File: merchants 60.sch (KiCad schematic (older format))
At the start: 182 parts, among them SW1 SW_PUSH, U1 ATmega32U4-AU, Y1 16MHz

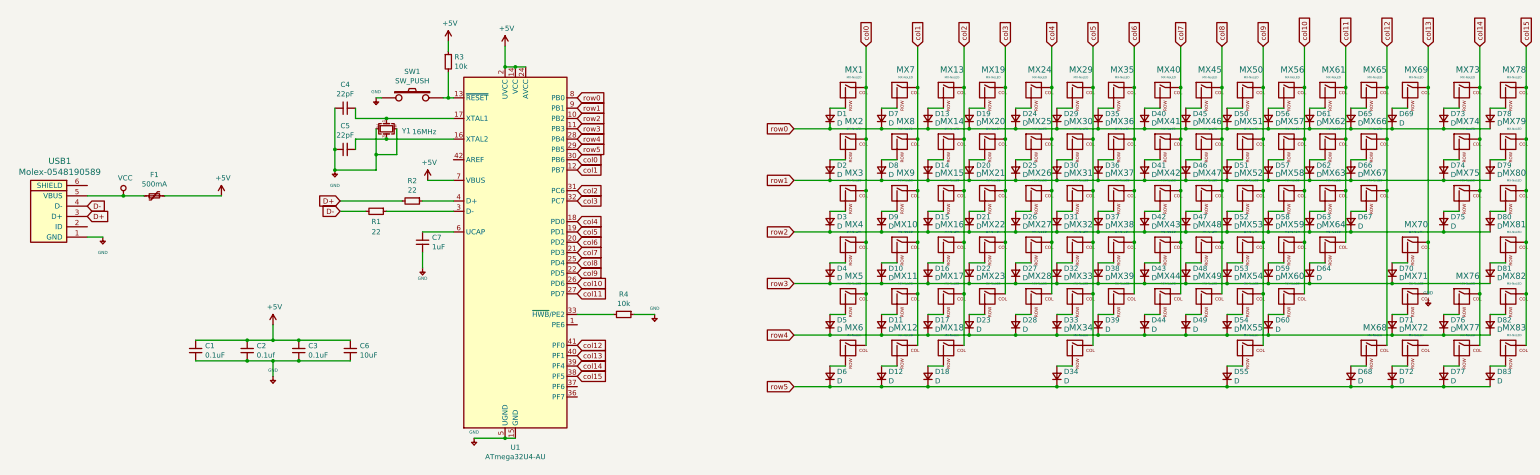
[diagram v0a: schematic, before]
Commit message: Finalising PCB and Generating Gerbers
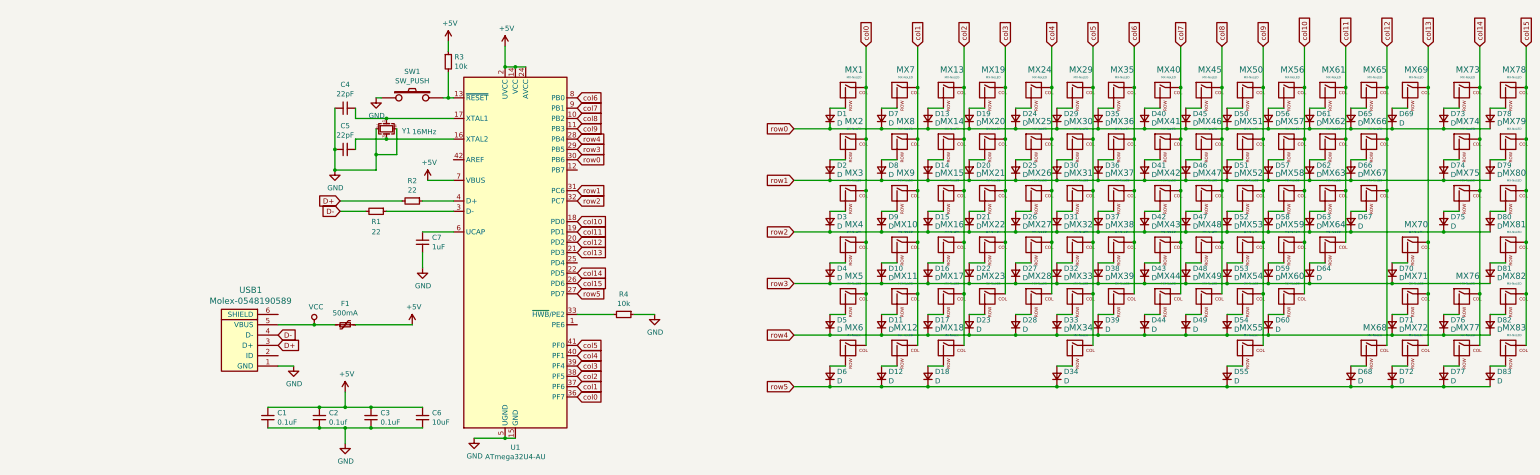
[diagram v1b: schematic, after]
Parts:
- D1, D10, D11, D12, D13, D14, D15, D16, D17, D18, D19, D2, D20, D21, D22, D23, D24, D25, D26, D27, D28, D29, D3, D30, D31, D32, D33, D34, D35, D36, D37, D38, D39, D4, D40, D41, D42, D43, D44, D45, D46, D47, D48, D49, D5, D50, D51, D52, D53, D54, D55, D56, D57, D58, D59, D6, D60, D61, D62, D63, D64, D65, D66, D67, D68, D69, D7, D70, D71, D72, D73, D74, D75, D76, D77, D78, D79, D8, D80, D81, D82, D83, D9: footprint Diode_SMD:D_SOD-123 -> keyboard_parts:D_SOD123_axial
- MX1, MX10, MX11, MX13, MX14, MX15, MX16, MX17, MX19, MX2, MX20, MX22, MX23, MX24, MX25, MX26, MX28, MX29, MX30, MX31, MX32, MX33, MX35, MX36, MX37, MX38, MX39, MX40, MX41, MX42, MX43, MX44, MX45, MX46, MX47, MX48, MX49, MX50, MX51, MX52, MX53, MX54, MX56, MX57, MX58, MX59, MX60, MX61, MX62, MX63, MX64, MX65, MX66, MX67, MX69, MX7, MX72, MX73, MX76, MX77, MX78, MX79, MX8, MX80, MX81, MX82, MX83, MX9: footprint (none) -> MX_Alps_Hybrid:MX-1U-NoLED
- MX12, MX18: footprint (none) -> MX_Alps_Hybrid:MX-1.25U-NoLED
- MX21, MX27: footprint MX_Alps_Hybrid:MX-1.25U -> MX_Alps_Hybrid:MX-1U-NoLED
- MX3, MX55, MX68, MX75: footprint MX_Alps_Hybrid:MX-1.5U -> MX_Alps_Hybrid:MX-1.5U-NoLED
- MX34: footprint MX_Alps_Hybrid:MX-6.25U -> MX_Alps_Hybrid:MX-6.25U-NoLED
- MX4, MX71: footprint MX_Alps_Hybrid:MX-1.75U -> MX_Alps_Hybrid:MX-1.75U-NoLED
- MX5: footprint MX_Alps_Hybrid:MX-2.5U -> MX_Alps_Hybrid:MX-2.25U-NoLED
- MX6: footprint MX_Alps_Hybrid:MX-1.25U -> MX_Alps_Hybrid:MX-1.25U-NoLED
- MX70: footprint MX_Alps_Hybrid:MX-2.25U -> MX_Alps_Hybrid:MX-2.25U-NoLED
- MX74: footprint MX_Alps_Hybrid:MX-2U -> MX_Alps_Hybrid:MX-2U-NoLED
- USB1: footprint random-keyboard-parts:Molex-0548190589 -> keyboard_parts:USB_miniB
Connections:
- net +5V: no longer C1.2, C2.2, C3.1, C4.2, C5.1, C6.2, C7.2, R4.1, SW1.1, U1.15 (GND), U1.23 (GND), U1.35 (GND), U1.43 (GND), U1.5 (UGND), USB1.1 (GND), Y1.2, Y1.4
- net col0: now also U1.36 (PF7); no longer U1.30 (PB6)
- net col1: now also U1.37 (PF6); no longer U1.12 (PB7)
- net col10: now also U1.18 (PD0); no longer U1.26 (PD6)
- net col11: now also U1.19 (PD1); no longer U1.27 (PD7)
- net col12: now also U1.20 (PD2); no longer U1.41 (PF0)
- net col13: now also MX72.1 (COL), U1.21 (PD3); no longer U1.40 (PF1)
- net col14: now also U1.22 (PD5); no longer U1.39 (PF4)
- net col15: now also U1.26 (PD6); no longer U1.38 (PF5)
- net col2: now also U1.38 (PF5); no longer U1.31 (PC6)
- net col3: now also U1.39 (PF4); no longer U1.32 (PC7)
- net col4: now also U1.40 (PF1); no longer U1.18 (PD0)
- net col5: now also U1.41 (PF0); no longer U1.19 (PD1)
- net col6: now also U1.8 (PB0); no longer U1.20 (PD2)
- net col7: now also U1.9 (PB1); no longer U1.21 (PD3)
- net col8: now also U1.10 (PB2); no longer U1.25 (PD4)
- net col9: now also U1.11 (PB3); no longer U1.22 (PD5)
- net row0: now also U1.30 (PB6); no longer U1.8 (PB0)
- net row1: now also U1.31 (PC6); no longer U1.9 (PB1)
- net row2: now also U1.32 (PC7); no longer U1.10 (PB2)
- net row3: now also U1.29 (PB5); no longer U1.11 (PB3)
- net row5: now also U1.27 (PD7); no longer U1.29 (PB5)
- new net GND: C1.2, C2.2, C3.1, C4.2, C5.1, C6.2, C7.2, R4.1, SW1.1, U1.15 (GND), U1.23 (GND), U1.35 (GND), U1.43 (GND), U1.5 (UGND), USB1.1 (GND), Y1.2, Y1.4
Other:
- moved on the sheet: C1, C2, C3, C6, F1, USB1

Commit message: Minor Changes
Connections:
- net row3: now also U1.27 (PD7); no longer U1.29 (PB5)
- net row5: now also U1.29 (PB5); no longer U1.27 (PD7)
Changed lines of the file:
@@
 row2
 Text GLabel 7550 2600 2    50   Input ~ 0
-row3
-Text GLabel 7550 2500 2    50   Input ~ 0
-row4
-Text GLabel 7550 4000 2    50   Input ~ 0
 row5
 Connection ~ 6850 5400
@@
 Text GLabel 7550 3900 2    50   Input ~ 0
 col15
-Text GLabel 7550 4500 2    50   Input ~ 0
-col5
 Text GLabel 7550 4600 2    50   Input ~ 0
 col4
@@
 Text GLabel 7550 4900 2    50   Input ~ 0
 col1
+Text GLabel 7550 4000 2    50   Input ~ 0
+row3
+Text GLabel 7550 2500 2    50   Input ~ 0
+row4
+Text GLabel 7550 4500 2    50   Input ~ 0
+col5
 $EndSCHEMATC

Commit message: Minor Changes
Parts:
- SW1: symbol keyboard_parts:SW_PUSH -> merchants-60-rescue:SW_PUSH-keyboard_parts
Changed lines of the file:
@@
 	5600 2650 5600 2400
 $Comp
-L keyboard_parts:SW_PUSH SW1
+L merchants-60-rescue:SW_PUSH-keyboard_parts SW1
 U 1 1 5F720C2E
 P 5950 2100

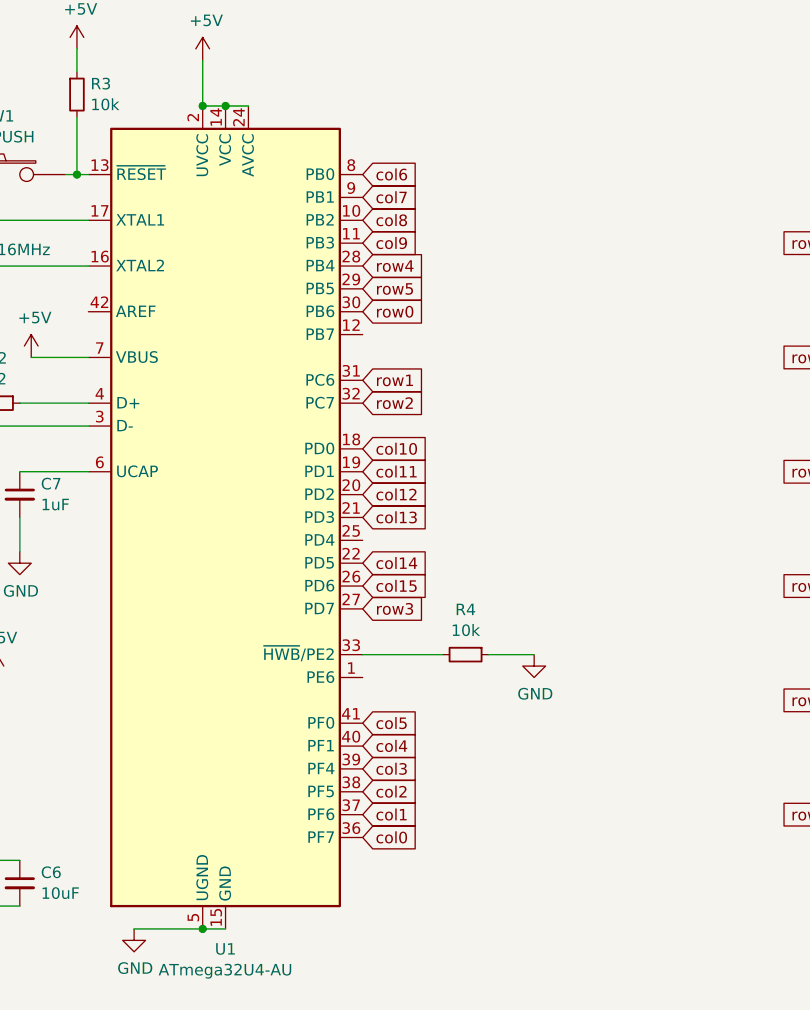
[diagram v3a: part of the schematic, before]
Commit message: Rerouting traces
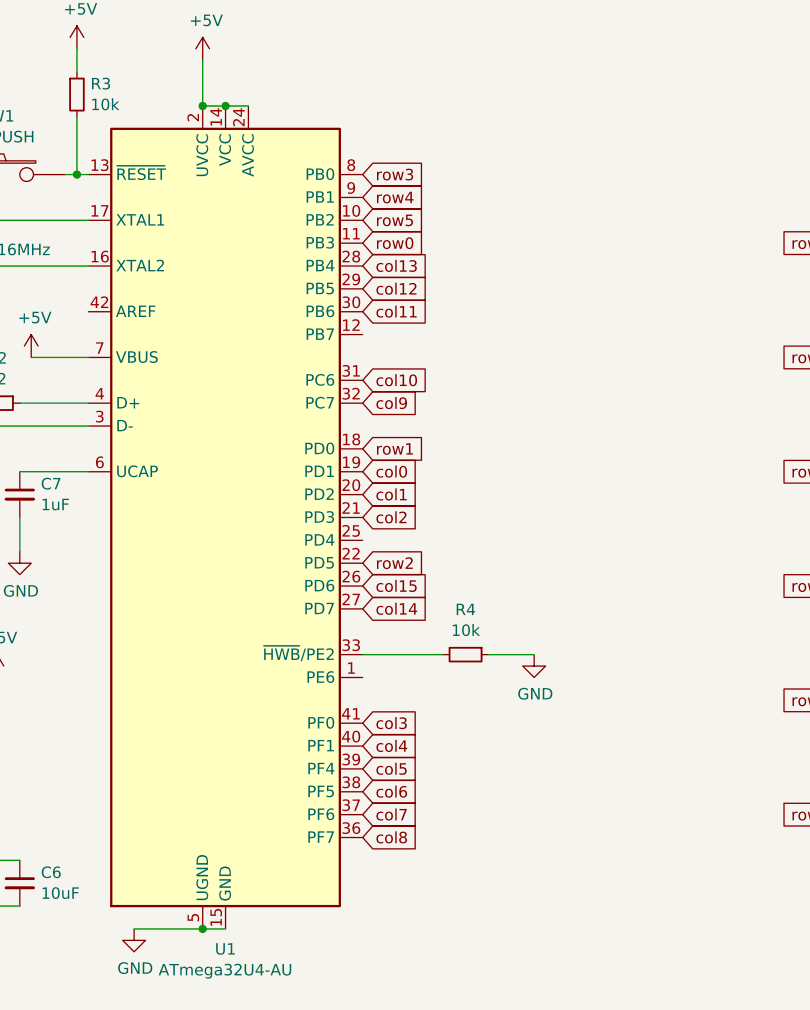
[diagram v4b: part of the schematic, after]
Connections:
- net col0: now also U1.19 (PD1); no longer U1.36 (PF7)
- net col1: now also U1.20 (PD2); no longer U1.37 (PF6)
- net col10: now also U1.31 (PC6); no longer U1.18 (PD0)
- net col11: now also U1.30 (PB6); no longer U1.19 (PD1)
- net col12: now also U1.29 (PB5); no longer U1.20 (PD2)
- net col13: now also U1.28 (PB4); no longer U1.21 (PD3)
- net col14: now also U1.27 (PD7); no longer U1.22 (PD5)
- net col2: now also U1.21 (PD3); no longer U1.38 (PF5)
- net col3: now also U1.41 (PF0); no longer U1.39 (PF4)
- net col5: now also U1.39 (PF4); no longer U1.41 (PF0)
- net col6: now also U1.38 (PF5); no longer U1.8 (PB0)
- net col7: now also U1.37 (PF6); no longer U1.9 (PB1)
- net col8: now also U1.36 (PF7); no longer U1.10 (PB2)
- net col9: now also U1.32 (PC7); no longer U1.11 (PB3)
- net row0: now also U1.11 (PB3); no longer U1.30 (PB6)
- net row1: now also U1.18 (PD0); no longer U1.31 (PC6)
- net row2: now also U1.22 (PD5); no longer U1.32 (PC7)
- net row3: now also U1.8 (PB0); no longer U1.27 (PD7)
- net row4: now also U1.9 (PB1); no longer U1.28 (PB4)
- net row5: now also U1.10 (PB2); no longer U1.29 (PB5)
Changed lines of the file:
@@
 Text GLabel 16750 1600 1    50   Input ~ 0
 col15
-Text GLabel 7550 2700 2    50   Input ~ 0
+Text GLabel 7550 2400 2    50   Input ~ 0
 row0
-Text GLabel 7550 3000 2    50   Input ~ 0
+Text GLabel 7550 3300 2    50   Input ~ 0
 row1
-Text GLabel 7550 3100 2    50   Input ~ 0
+Text GLabel 7550 3800 2    50   Input ~ 0
 row2
-Text GLabel 7550 2600 2    50   Input ~ 0
+Text GLabel 7550 2300 2    50   Input ~ 0
 row5
 Connection ~ 6850 5400
@@
 	1    0    0    -1
 $EndComp
-Text GLabel 7550 5000 2    50   Input ~ 0
+Text GLabel 7550 3400 2    50   Input ~ 0
 col0
-Text GLabel 7550 4800 2    50   Input ~ 0
+Text GLabel 7550 3600 2    50   Input ~ 0
 col2
-Text GLabel 7550 4700 2    50   Input ~ 0
+Text GLabel 7550 4500 2    50   Input ~ 0
 col3
-Text GLabel 7550 3400 2    50   Input ~ 0
+Text GLabel 7550 2700 2    50   Input ~ 0
 col11
 Wire Wire Line
@@
 $EndComp
 Connection ~ 5200 2800
-Text GLabel 7550 3500 2    50   Input ~ 0
+Text GLabel 7550 2600 2    50   Input ~ 0
 col12
-Text GLabel 7550 3600 2    50   Input ~ 0
+Text GLabel 7550 2500 2    50   Input ~ 0
 col13
-Text GLabel 7550 3800 2    50   Input ~ 0
+Text GLabel 7550 4000 2    50   Input ~ 0
 col14
 Text GLabel 7550 3900 2    50   Input ~ 0
@@
 Text GLabel 7550 4600 2    50   Input ~ 0
 col4
-Text GLabel 7550 3300 2    50   Input ~ 0
+Text GLabel 7550 5000 2    50   Input ~ 0
+col8
+Text GLabel 7550 4900 2    50   Input ~ 0
+col7
+Text GLabel 7550 4800 2    50   Input ~ 0
+col6
+Text GLabel 7550 3500 2    50   Input ~ 0
+col1
+Text GLabel 7550 2100 2    50   Input ~ 0
+row3
+Text GLabel 7550 2200 2    50   Input ~ 0
+row4
+Text GLabel 7550 4700 2    50   Input ~ 0
+col5
+Text GLabel 7550 3000 2    50   Input ~ 0
 col10
-Text GLabel 7550 2400 2    50   Input ~ 0
+Text GLabel 7550 3100 2    50   Input ~ 0
 col9
-Text GLabel 7550 2300 2    50   Input ~ 0
-col8
-Text GLabel 7550 2200 2    50   Input ~ 0
-col7
-Text GLabel 7550 2100 2    50   Input ~ 0
-col6
-Text GLabel 7550 4900 2    50   Input ~ 0
-col1
-Text GLabel 7550 4000 2    50   Input ~ 0
-row3
-Text GLabel 7550 2500 2    50   Input ~ 0
-row4
-Text GLabel 7550 4500 2    50   Input ~ 0
-col5
 $EndSCHEMATC
